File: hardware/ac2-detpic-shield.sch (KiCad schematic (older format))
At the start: 38 parts

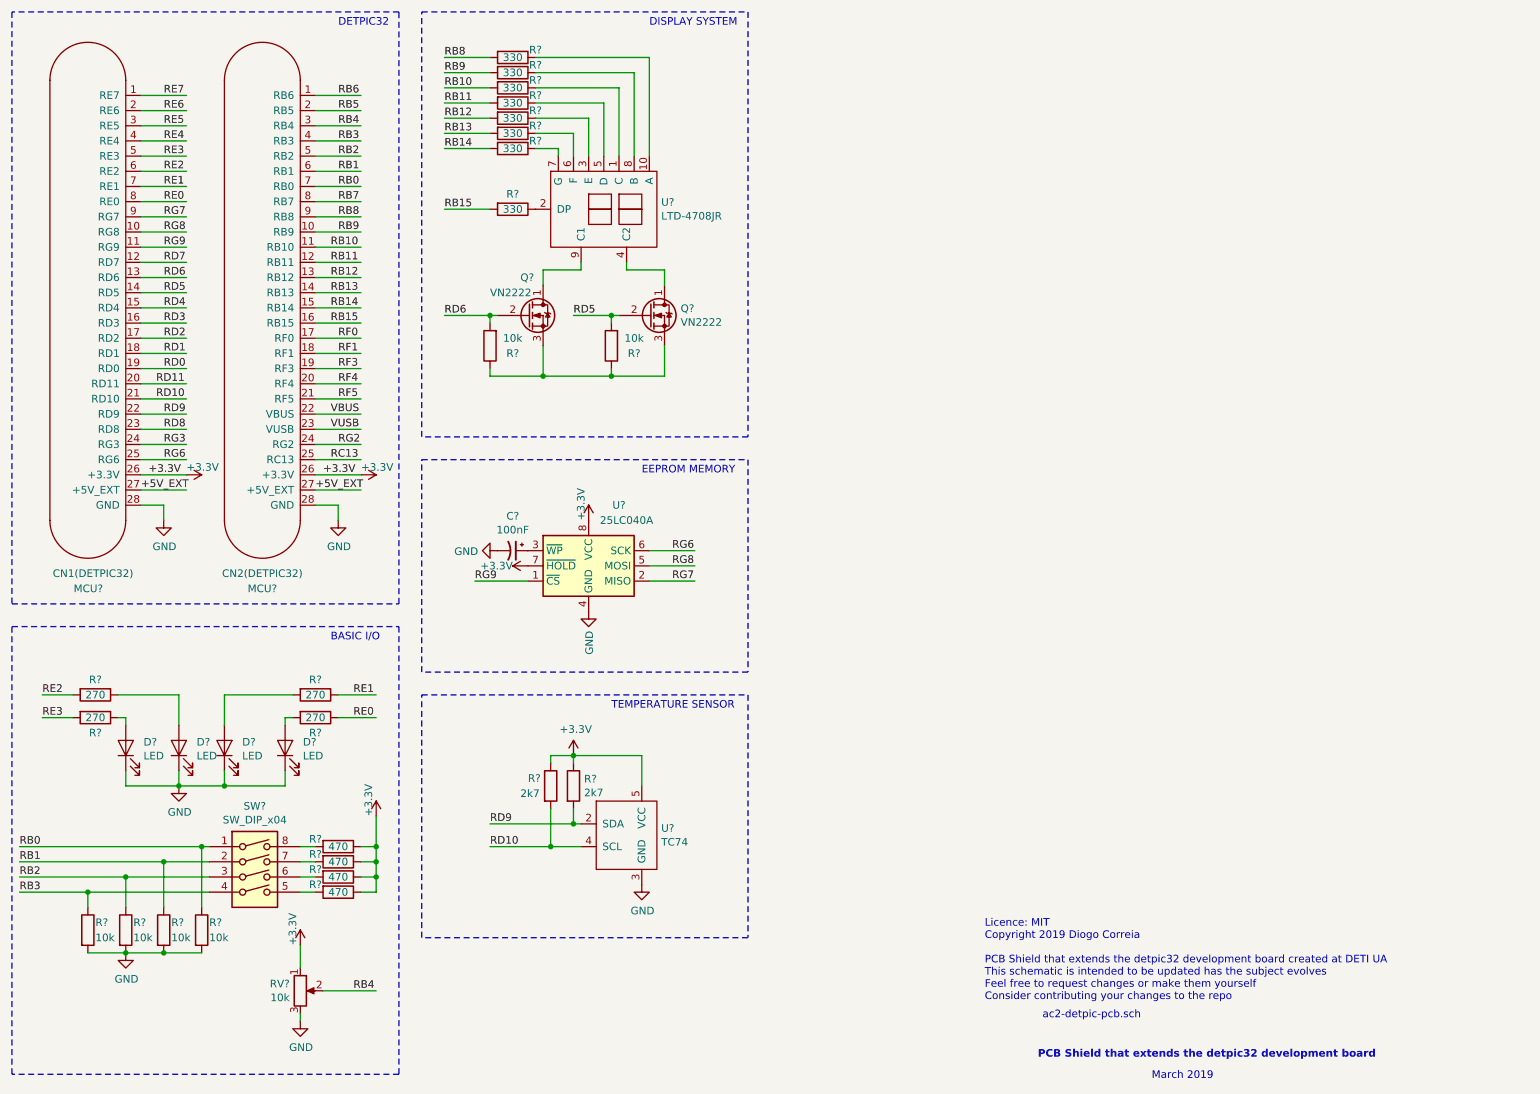
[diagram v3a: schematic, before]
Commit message: LTD-4708JR footprint created and footprints assigment completed
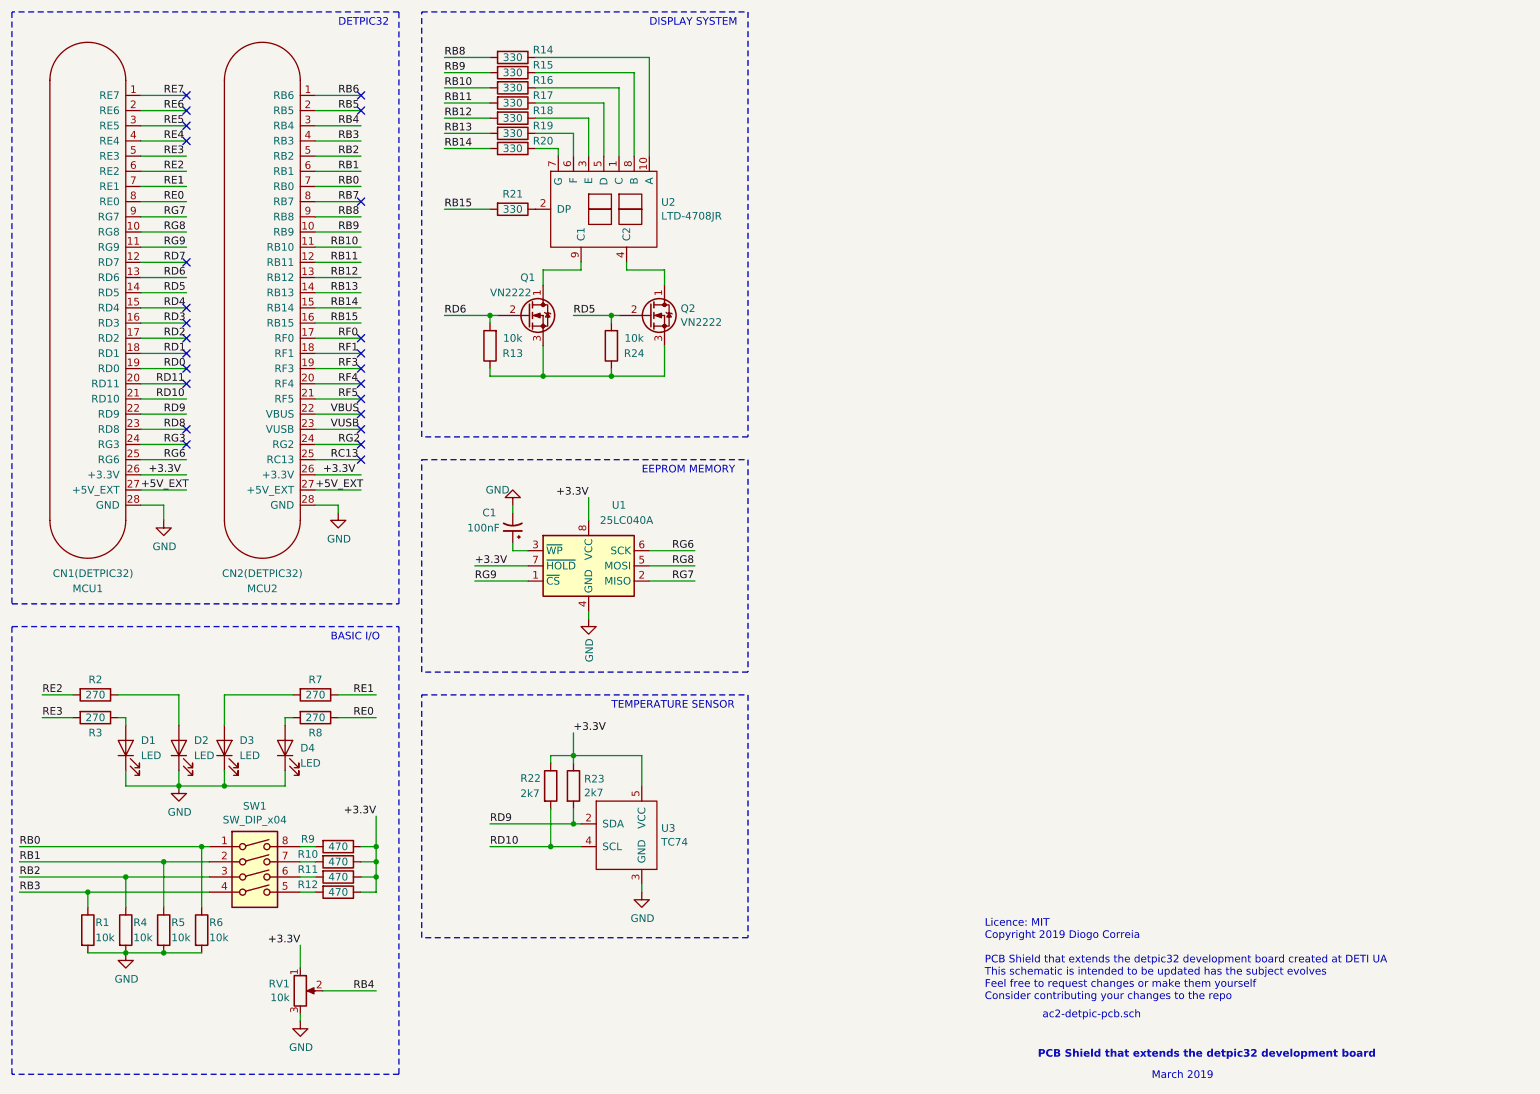
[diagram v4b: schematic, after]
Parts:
- removed U?: TC74, symbol ac2-detpic-shield:TC74
- added U3: TC74, Package_TO_SOT_THT:TO-220-5_Horizontal_TabDown, symbol ac2-detpic-shield:TC74
- C1: renamed from C?; footprint (none) -> Capacitor_THT:CP_Radial_D7.5mm_P2.50mm
- D1, D2, D3, D4: renamed from D?; footprint (none) -> LED_THT:LED_D3.0mm
- MCU1, MCU2: renamed from MCU?; footprint (none) -> Connector_PinHeader_2.54mm:PinHeader_1x28_P2.54mm_Vertical
- Q1, Q2: renamed from Q?; footprint (none) -> Package_TO_SOT_THT:TO-92
- R1, R10, R11, R12, R13, R14, R15, R16, R17, R18, R19, R2, R20, R21, R22, R23, R24, R3, R4, R5, R6, R7, R8, R9: renamed from R?; footprint (none) -> Resistor_THT:R_Axial_DIN0207_L6.3mm_D2.5mm_P7.62mm_Horizontal
- RV1: renamed from RV?; footprint (none) -> Potentiometer_THT:Potentiometer_ACP_CA14V-15_Vertical
- SW1: renamed from SW?; footprint (none) -> Button_Switch_THT:SW_DIP_SPSTx04_Slide_9.78x12.34mm_W7.62mm_P2.54mm
- U1: renamed from U?; footprint (none) -> Package_DIP:DIP-8_W7.62mm_Socket_LongPads
- U2: renamed from U?; footprint (none) -> LTD-4708JR:LTD-4708JR
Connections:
- wire segments 163 -> 171
- no-connect marks 0 -> 25
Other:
- moved on the sheet: C1

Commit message: file structure in docs changed + pcb layout and detpic aux info done
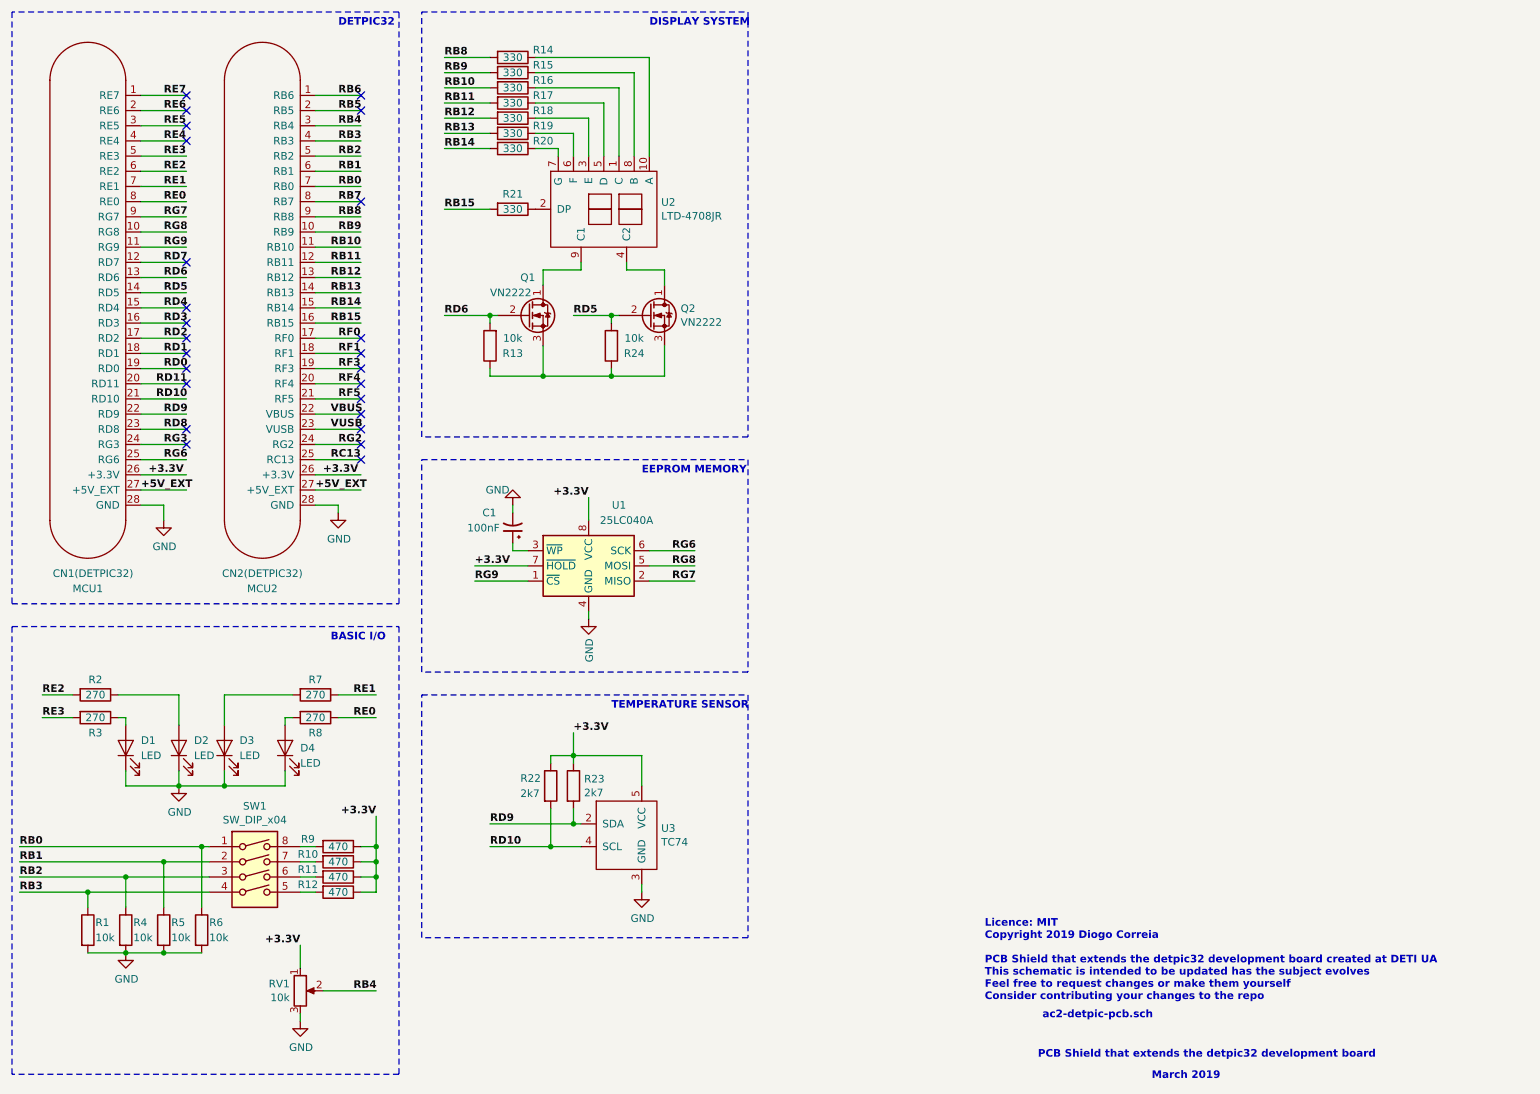
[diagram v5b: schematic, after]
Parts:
- MCU1, MCU2: footprint Connector_PinHeader_2.54mm:PinHeader_1x28_P2.54mm_Vertical -> Connector_PinSocket_2.54mm:PinSocket_1x28_P2.54mm_Vertical
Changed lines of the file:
@@
 Comment4 ""
 $EndDescr
-Text Notes 7010 7120 0    50   ~ 0
+Text Notes 7010 7120 0    50   ~ 6
 Licence: MIT\nCopyright 2019 Diogo Correia\n\nPCB Shield that extends the detpic32 development board created at DETI UA\nThis schematic is intended to be updated has the subject evolves\nFeel free to request changes or make them yourself\nConsider contributing your changes to the repo
-Text Notes 7390 7240 0    50   ~ 0
+Text Notes 7390 7240 0    50   ~ 6
 ac2-detpic-pcb.sch
 Text Notes 7360 7500 0    50   ~ 10
 PCB Shield that extends the detpic32 development board
-Text Notes 8110 7640 0    50   ~ 0
+Text Notes 8110 7640 0    50   ~ 6
 March 2019
 $Comp
@@
 F 0 "MCU1" H 1200 600 50  0000 R CNN
 F 1 "CN1(DETPIC32)" H 1400 700 50  0000 R CNN
-F 2 "Connector_PinHeader_2.54mm:PinHeader_1x28_P2.54mm_Vertical" H 1150 2500 50  0001 C CNN
+F 2 "Connector_PinSocket_2.54mm:PinSocket_1x28_P2.54mm_Vertical" H 1150 2500 50  0001 C CNN
 F 3 "" H 1150 2500 50  0001 C CNN
 	1    1150 2500
@@
 F 0 "MCU2" H 2250 600 50  0000 C CNN
 F 1 "CN2(DETPIC32)" H 2250 700 50  0000 C CNN
-F 2 "Connector_PinHeader_2.54mm:PinHeader_1x28_P2.54mm_Vertical" V 2600 1450 50  0001 C CNN
+F 2 "Connector_PinSocket_2.54mm:PinSocket_1x28_P2.54mm_Vertical" V 2600 1450 50  0001 C CNN
 F 3 "" V 2600 1450 50  0001 C CNN
 	1    2400 2500
@@
 Wire Wire Line
 	2600 3750 2900 3750
-Text Label 1600 1150 0    50   ~ 0
+Text Label 1600 1150 0    50   ~ 6
 RE7
-Text Label 1600 1250 0    50   ~ 0
+Text Label 1600 1250 0    50   ~ 6
 RE6
-Text Label 1600 1350 0    50   ~ 0
+Text Label 1600 1350 0    50   ~ 6
 RE5
-Text Label 1600 1450 0    50   ~ 0
+Text Label 1600 1450 0    50   ~ 6
 RE4
-Text Label 1600 1550 0    50   ~ 0
+Text Label 1600 1550 0    50   ~ 6
 RE3
-Text Label 1600 1650 0    50   ~ 0
+Text Label 1600 1650 0    50   ~ 6
 RE2
-Text Label 1600 1750 0    50   ~ 0
+Text Label 1600 1750 0    50   ~ 6
 RE1
-Text Label 1600 1850 0    50   ~ 0
+Text Label 1600 1850 0    50   ~ 6
 RE0
-Text Label 1600 1950 0    50   ~ 0
+Text Label 1600 1950 0    50   ~ 6
 RG7
-Text Label 1600 2050 0    50   ~ 0
+Text Label 1600 2050 0    50   ~ 6
 RG8
-Text Label 1600 2150 0    50   ~ 0
+Text Label 1600 2150 0    50   ~ 6
 RG9
-Text Label 1600 2250 0    50   ~ 0
+Text Label 1600 2250 0    50   ~ 6
 RD7
-Text Label 1600 2350 0    50   ~ 0
+Text Label 1600 2350 0    50   ~ 6
 RD6
-Text Label 1600 2450 0    50   ~ 0
+Text Label 1600 2450 0    50   ~ 6
 RD5
-Text Label 1600 2550 0    50   ~ 0
+Text Label 1600 2550 0    50   ~ 6
 RD4
-Text Label 1600 2650 0    50   ~ 0
+Text Label 1600 2650 0    50   ~ 6
 RD3
-Text Label 1600 2750 0    50   ~ 0
+Text Label 1600 2750 0    50   ~ 6
 RD2
-Text Label 1600 2850 0    50   ~ 0
+Text Label 1600 2850 0    50   ~ 6
 RD1
-Text Label 1600 2950 0    50   ~ 0
+Text Label 1600 2950 0    50   ~ 6
 RD0
-Text Label 1550 3050 0    50   ~ 0
+Text Label 1550 3050 0    50   ~ 6
 RD11
-Text Label 1550 3150 0    50   ~ 0
+Text Label 1550 3150 0    50   ~ 6
 RD10
-Text Label 1600 3250 0    50   ~ 0
+Text Label 1600 3250 0    50   ~ 6
 RD9
-Text Label 1600 3350 0    50   ~ 0
+Text Label 1600 3350 0    50   ~ 6
 RD8
-Text Label 1600 3450 0    50   ~ 0
+Text Label 1600 3450 0    50   ~ 6
 RG3
-Text Label 1600 3550 0    50   ~ 0
+Text Label 1600 3550 0    50   ~ 6
 RG6
-Text Label 1500 3650 0    50   ~ 0
+Text Label 1500 3650 0    50   ~ 6
 +3.3V
-Text Label 1450 3750 0    50   ~ 0
+Text Label 1450 3750 0    50   ~ 6
 +5V_EXT
-Text Label 2750 1150 0    50   ~ 0
+Text Label 2750 1150 0    50   ~ 6
 RB6
-Text Label 2750 1250 0    50   ~ 0
+Text Label 2750 1250 0    50   ~ 6
 RB5
-Text Label 2750 1350 0    50   ~ 0
+Text Label 2750 1350 0    50   ~ 6
 RB4
-Text Label 2750 1450 0    50   ~ 0
+Text Label 2750 1450 0    50   ~ 6
 RB3
-Text Label 2750 1550 0    50   ~ 0
+Text Label 2750 1550 0    50   ~ 6
 RB2
-Text Label 2750 1650 0    50   ~ 0
+Text Label 2750 1650 0    50   ~ 6
 RB1
-Text Label 2750 1750 0    50   ~ 0
+Text Label 2750 1750 0    50   ~ 6
 RB0
-Text Label 2750 1850 0    50   ~ 0
+Text Label 2750 1850 0    50   ~ 6
 RB7
-Text Label 2750 1950 0    50   ~ 0
+Text Label 2750 1950 0    50   ~ 6
 RB8
-Text Label 2750 2050 0    50   ~ 0
+Text Label 2750 2050 0    50   ~ 6
 RB9
-Text Label 2700 2150 0    50   ~ 0
+Text Label 2700 2150 0    50   ~ 6
 RB10
-Text Label 2700 2250 0    50   ~ 0
+Text Label 2700 2250 0    50   ~ 6
 RB11
-Text Label 2700 2350 0    50   ~ 0
+Text Label 2700 2350 0    50   ~ 6
 RB12
-Text Label 2700 2450 0    50   ~ 0
+Text Label 2700 2450 0    50   ~ 6
 RB13
-Text Label 2700 2550 0    50   ~ 0
+Text Label 2700 2550 0    50   ~ 6
 RB14
-Text Label 2700 2650 0    50   ~ 0
+Text Label 2700 2650 0    50   ~ 6
 RB15
-Text Label 2750 2750 0    50   ~ 0
+Text Label 2750 2750 0    50   ~ 6
 RF0
-Text Label 2750 2850 0    50   ~ 0
+Text Label 2750 2850 0    50   ~ 6
 RF1
-Text Label 2750 2950 0    50   ~ 0
+Text Label 2750 2950 0    50   ~ 6
 RF3
-Text Label 2750 3050 0    50   ~ 0
+Text Label 2750 3050 0    50   ~ 6
 RF4
-Text Label 2750 3150 0    50   ~ 0
+Text Label 2750 3150 0    50   ~ 6
 RF5
-Text Label 2700 3250 0    50   ~ 0
+Text Label 2700 3250 0    50   ~ 6
 VBUS
-Text Label 2700 3350 0    50   ~ 0
+Text Label 2700 3350 0    50   ~ 6
 VUSB
-Text Label 2750 3450 0    50   ~ 0
+Text Label 2750 3450 0    50   ~ 6
 RG2
-Text Label 2700 3550 0    50   ~ 0
+Text Label 2700 3550 0    50   ~ 6
 RC13
-Text Label 2650 3650 0    50   ~ 0
+Text Label 2650 3650 0    50   ~ 6
 +3.3V
-Text Label 2600 3750 0    50   ~ 0
+Text Label 2600 3750 0    50   ~ 6
 +5V_EXT
 Wire Notes Line
@@
 Wire Notes Line
 	3150 600  600  600
-Text Notes 2750 700  0    50   ~ 0
+Text Notes 2750 700  0    50   ~ 6
 DETPIC32
 Wire Wire Line
@@
 Wire Wire Line
 	2750 5250 3000 5250
-Text Label 800  5100 0    50   ~ 0
+Text Label 800  5100 0    50   ~ 6
 RE2
-Text Label 800  5250 0    50   ~ 0
+Text Label 800  5250 0    50   ~ 6
 RE3
-Text Label 2850 5100 0    50   ~ 0
+Text Label 2850 5100 0    50   ~ 6
 RE1
-Text Label 2850 5250 0    50   ~ 0
+Text Label 2850 5250 0    50   ~ 6
 RE0
 Wire Wire Line
@@
 Wire Wire Line
 	3000 6100 3000 5900
-Text Label 650  6100 0    50   ~ 0
+Text Label 650  6100 0    50   ~ 6
 RB0
-Text Label 650  6200 0    50   ~ 0
+Text Label 650  6200 0    50   ~ 6
 RB1
-Text Label 650  6300 0    50   ~ 0
+Text Label 650  6300 0    50   ~ 6
 RB2
-Text Label 650  6400 0    50   ~ 0
+Text Label 650  6400 0    50   ~ 6
 RB3
 Wire Wire Line
@@
 Wire Wire Line
 	2500 6900 2500 6750
-Text Label 2850 7050 0    50   ~ 0
+Text Label 2850 7050 0    50   ~ 6
 RB4
 Wire Notes Line
@@
 Wire Notes Line
 	600  7600 600  4650
-Text Notes 2700 4750 0    50   ~ 0
+Text Notes 2700 4750 0    50   ~ 6
 BASIC I/O
 Wire Wire Line
@@
 Wire Wire Line
 	3750 1500 3450 1500
-Text Label 3450 900  0    50   ~ 0
+Text Label 3450 900  0    50   ~ 6
 RB8
-Text Label 3450 1000 0    50   ~ 0
+Text Label 3450 1000 0    50   ~ 6
 RB9
-Text Label 3450 1100 0    50   ~ 0
+Text Label 3450 1100 0    50   ~ 6
 RB10
-Text Label 3450 1200 0    50   ~ 0
+Text Label 3450 1200 0    50   ~ 6
 RB11
-Text Label 3450 1300 0    50   ~ 0
+Text Label 3450 1300 0    50   ~ 6
 RB12
-Text Label 3450 1400 0    50   ~ 0
+Text Label 3450 1400 0    50   ~ 6
 RB13
-Text Label 3450 1500 0    50   ~ 0
+Text Label 3450 1500 0    50   ~ 6
 RB14
 $Comp
@@
 Wire Wire Line
 	3750 1900 3450 1900
-Text Label 3450 1900 0    50   ~ 0
+Text Label 3450 1900 0    50   ~ 6
 RB15
 Wire Wire Line
@@
 	4100 2800 4100 3000
 Connection ~ 4100 3000
-Text Label 4300 2600 0    50   ~ 0
+Text Label 4300 2600 0    50   ~ 6
 RD5
-Text Label 3450 2600 0    50   ~ 0
+Text Label 3450 2600 0    50   ~ 6
 RD6
 Wire Wire Line
@@
 Wire Notes Line
 	3300 3400 3300 600
-Text Notes 4800 700  0    50   ~ 0
+Text Notes 4800 700  0    50   ~ 6
 DISPLAY SYSTEM
 $Comp
@@
 Wire Wire Line
 	4000 4350 3650 4350
-Text Label 3650 4350 0    50   ~ 0
+Text Label 3650 4350 0    50   ~ 6
 RG9
 $Comp
@@
 Wire Wire Line
 	4800 4350 5100 4350
-Text Label 4950 4150 0    50   ~ 0
+Text Label 4950 4150 0    50   ~ 6
 RG6
-Text Label 4950 4250 0    50   ~ 0
+Text Label 4950 4250 0    50   ~ 6
 RG8
-Text Label 4950 4350 0    50   ~ 0
+Text Label 4950 4350 0    50   ~ 6
 RG7
 Wire Notes Line
@@
 Wire Notes Line
 	3300 4950 3300 3550
-Text Notes 4750 3650 0    50   ~ 0
+Text Notes 4750 3650 0    50   ~ 6
 EEPROM MEMORY
 $Comp
@@
 	4150 6100 3750 6100
 Connection ~ 4150 6100
-Text Label 3750 5950 0    50   ~ 0
+Text Label 3750 5950 0    50   ~ 6
 RD9
-Text Label 3750 6100 0    50   ~ 0
+Text Label 3750 6100 0    50   ~ 6
 RD10
 Wire Notes Line
@@
 Wire Notes Line
 	3300 6700 3300 5100
-Text Notes 4550 5200 0    50   ~ 0
+Text Notes 4550 5200 0    50   ~ 6
 TEMPERATURE SENSOR
 Wire Wire Line
@@
 Wire Wire Line
 	1450 3550 1750 3550
-Text Label 3000 5900 2    50   ~ 0
+Text Label 3000 5900 2    50   ~ 6
 +3.3V
-Text Label 2500 6750 2    50   ~ 0
+Text Label 2500 6750 2    50   ~ 6
 +3.3V
 Wire Wire Line
 	4300 5500 4300 5350
-Text Label 4300 5350 0    50   ~ 0
+Text Label 4300 5350 0    50   ~ 6
 +3.3V
 Wire Wire Line
 	4400 3950 4400 3800
-Text Label 4400 3800 2    50   ~ 0
+Text Label 4400 3800 2    50   ~ 6
 +3.3V
 Wire Wire Line
 	4000 4250 3650 4250
-Text Label 3650 4250 0    50   ~ 0
+Text Label 3650 4250 0    50   ~ 6
 +3.3V
 Wire Wire Line

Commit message: pcb completed + gerbers exported
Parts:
- added J1: HEADER, Connector_PinHeader_2.54mm:PinHeader_1x04_P2.54mm_Vertical, symbol Connector:Conn_01x04_Male
- added J2, J6: HEADER, Connector_PinHeader_2.54mm:PinHeader_1x01_P2.54mm_Vertical, symbol Connector:Conn_01x01_Male
- added J3: HEADER, Connector_PinHeader_2.54mm:PinHeader_1x07_P2.54mm_Vertical, symbol Connector:Conn_01x07_Male
- added J4, J5: HEADER, Connector_PinHeader_2.54mm:PinHeader_1x02_P2.54mm_Vertical, symbol Connector:Conn_01x02_Male
- added J7: HEADER, Connector_PinHeader_2.54mm:PinHeader_1x09_P2.54mm_Vertical, symbol Connector:Conn_01x09_Male
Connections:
- net labels added: +5V_EXT1, +5V_EXT2
- net labels removed: +5V_EXT
- no-connect marks 25 -> 2
